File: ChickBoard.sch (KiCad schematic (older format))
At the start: 12 parts, among them CON1 AVR-ISP-6, J1 Screw_Terminal_1x04, J2 CONN_01X02, J3 CONN_01X02, J4 CONN_01X02, Q1 Q_NMOS_DGS, Q2 Q_PMOS_DGS, U1 ATMEGA328-AU, U2 SN65HVD485E, U3 RFID, U4 AMS1117

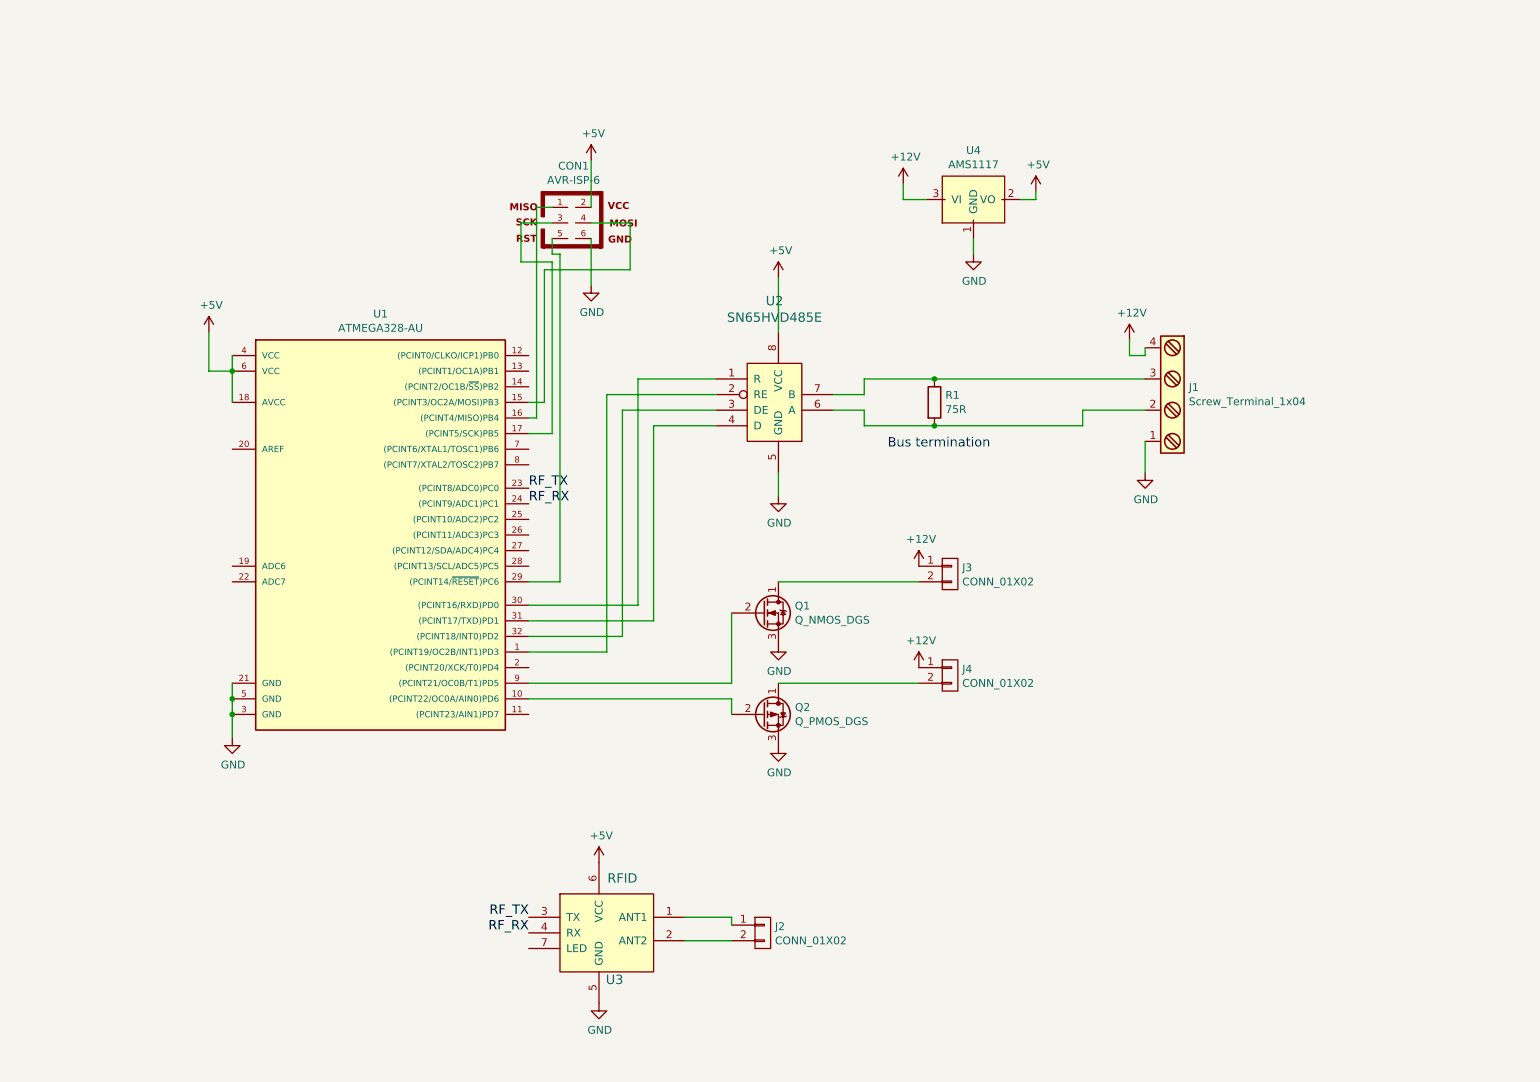
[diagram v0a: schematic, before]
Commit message: Switched to SAMD20 mcu
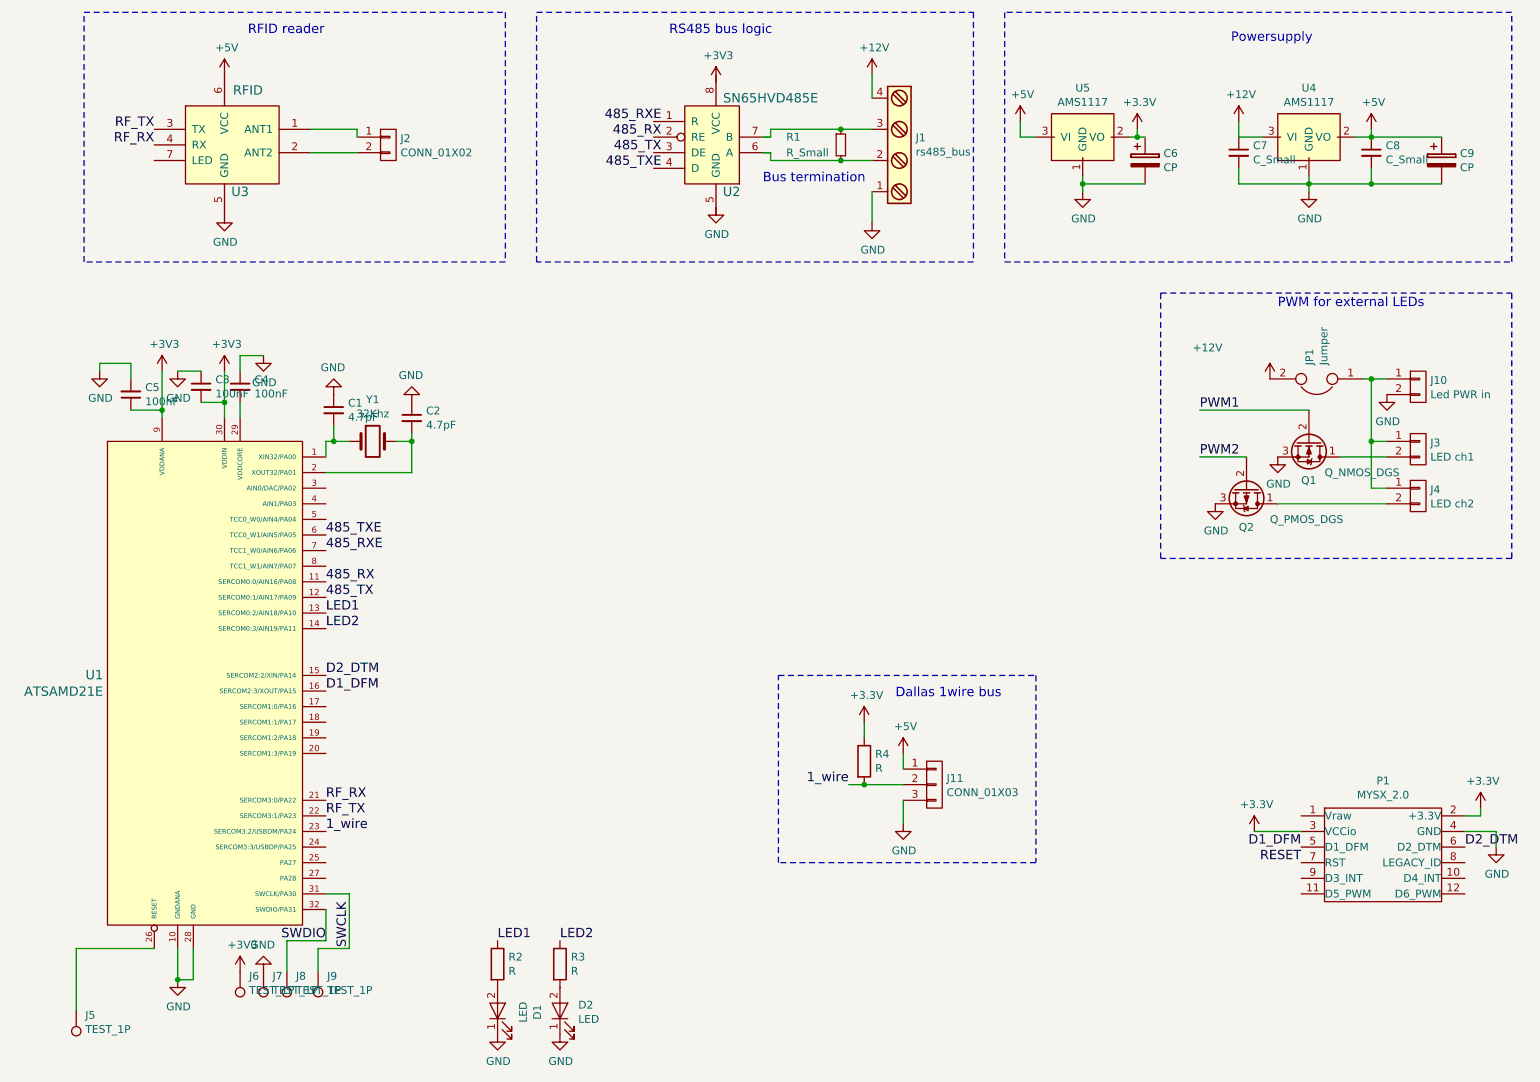
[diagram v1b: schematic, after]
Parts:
- removed CON1: AVR-ISP-6, Pin_Headers:Pin_Header_Straight_2x03, symbol AVR-ISP-6
- removed R1: 75R, Resistors_SMD:R_0805_HandSoldering, symbol R
- removed U1: ATMEGA328-AU, Housings_QFP:TQFP-32_7x7mm_Pitch0.8mm, symbol ATMEGA328-AU
- added C1, C2: 4.7pF, Capacitors_SMD:C_0603_HandSoldering, symbol C_Small
- added C3, C4, C5: 100nF, Capacitors_SMD:C_0603_HandSoldering, symbol C_Small
- added C6, C9: CP, Capacitors_SMD:C_0603_HandSoldering, symbol CP
- added C7, C8: C_Small, Capacitors_SMD:C_0603_HandSoldering, symbol C_Small
- added D1, D2: LED, LEDs:LED-0603, symbol LED
- added J10: Led PWR in, Terminal_Blocks:TerminalBlock_Pheonix_MPT-2.54mm_2pol, symbol CONN_01X02
- added J11: CONN_01X03, Terminal_Blocks:TerminalBlock_Pheonix_MPT-2.54mm_3pol, symbol CONN_01X03
- added J5, J6, J7, J8, J9: TEST_1P, Measurement_Points:Measurement_Point_Round-SMD-Pad_Small, symbol TEST_1P
- added JP1: Jumper, mysensors_obscurities:2_pin_solder_jumper_smd, symbol Jumper
- added P1: MYSX_2.0, mysensors_connectors:MYSX_2.2, symbol MYSX_2.2
- added R1: R_Small, Resistors_SMD:R_0603_HandSoldering, symbol R_Small
- added R2, R3, R4: R, Resistors_SMD:R_0603_HandSoldering, symbol R
- added U1: ATSAMD21E, Housings_QFP:TQFP-32_7x7mm_Pitch0.8mm, symbol ATSAMD21E
- added U5: AMS1117, TO_SOT_Packages_SMD:SOT-23, symbol AMS1117
- added Y1: 32Khz, mysensors_obscurities:XTAL_3.2x1.5mm, symbol Crystal
- J1: value Screw_Terminal_1x04 -> rs485_bus
- J3: value CONN_01X02 -> LED ch1; footprint Pin_Headers:Pin_Header_Straight_1x02 -> Terminal_Blocks:TerminalBlock_Pheonix_MPT-2.54mm_2pol
- J4: value CONN_01X02 -> LED ch2; footprint Pin_Headers:Pin_Header_Straight_1x02 -> Terminal_Blocks:TerminalBlock_Pheonix_MPT-2.54mm_2pol
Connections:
- net +12V: now also C7.1, JP1.2; no longer J3.1 (P1), J4.1 (P1)
- net +5V: now also C8.1, C9.1, J11.1 (P1), U5.3 (VI); no longer U2.8 (VCC)
- net GND: now also C1.1, C2.1, C3.1, C4.1, C5.2, C6.2, C7.2, C8.2, C9.2, D1.1 (K), D2.1 (K), J10.2 (P2), J11.3 (P3), J7.1, P1.4 (GND), U1.10 (GNDANA), U1.28 (GND), U5.1 (GND); no longer U2.5 (GND)
- net RF_RX: now also U1.21 (SERCOM3:0/PA22)
- net RF_TX: now also U1.22 (SERCOM3:1/PA23)
- net PWM2: now reaches Q2.2 (G)
- net PWM1: now reaches Q1.2 (G)
- net at J1.2, U2.6 (A): now also R1.2
- net at J1.3, U2.7 (B): now also R1.1
- new net: J10.1 (P1), J3.1 (P1), J4.1 (P1), JP1.1
- new net: C1.2, U1.1 (XIN32/PA00), Y1.1
- new net: C2.2, U1.2 (XOUT32/PA01), Y1.2
- new net: J5.1, U1.26 (RESET)
- new net: C4.2, U1.29 (VDDCORE)
- new net: D1.2 (A), R2.2
- new net: D2.2 (A), R3.2
- new net +3V3: C3.2, C5.1, C6.1, J6.1, P1.2 (+3.3V), P1.3 (VCCio), R4.1, U1.30 (VDDIN), U1.9 (VDDANA), U5.2 (VO)
- new net 1_wire: J11.2 (P2), R4.2, U1.23 (SERCOM3:2/USBDM/PA24)
- new net 485_RX: U1.11 (SERCOM0:0/AIN16/PA08)
- new net 485_RXE: U1.7 (TCC1_W0/AIN6/PA06)
- new net 485_TX: U1.12 (SERCOM0:1/AIN17/PA09)
- new net 485_TXE: U1.6 (TCC0_W1/AIN5/PA05)
- new net D1_DFM: P1.5 (D1_DFM), U1.16 (SERCOM2:3/XOUT/PA15)
- new net D2_DTM: P1.6 (D2_DTM), U1.15 (SERCOM2:2/XIN/PA14)
- new net LED1: R2.1, U1.13 (SERCOM0:2/AIN18/PA10)
- new net LED2: R3.1, U1.14 (SERCOM0:3/AIN19/PA11)
- new net RESET: P1.7 (RST)
- new net SWCLK: J9.1, U1.31 (SWCLK/PA30)
- new net SWDIO: J8.1, U1.32 (SWDIO/PA31)
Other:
- note added: "Dallas 1wire bus"
- note added: "PWM for external LEDs"
- note added: "Powersupply"
- note added: "RFID reader"
- note added: "RS485 bus logic"
- moved on the sheet: J1, J2, J3, J4, Q1, Q2, U2, U3, U4
